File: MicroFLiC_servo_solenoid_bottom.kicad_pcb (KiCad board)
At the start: 2 copper layers, 49.8 x 49.8 mm, 49 parts, among them P1 Header_1x14, P10 Socket_1x4, P11 Header_R/A_2x3, P12 Header_R/A_2x3, P2 Socket_1x14, P3 12-way Micro-MaTch, P4 Jack_3.5mm_3pin, P5 Jack_3.5mm_3pin, P6 RCA_3, P7 RCA_3, P8 Socket_1x6, P9 Header_1x4, U1 PCA9306, U2 DRV103, U3 DRV103, U4 MCP4728

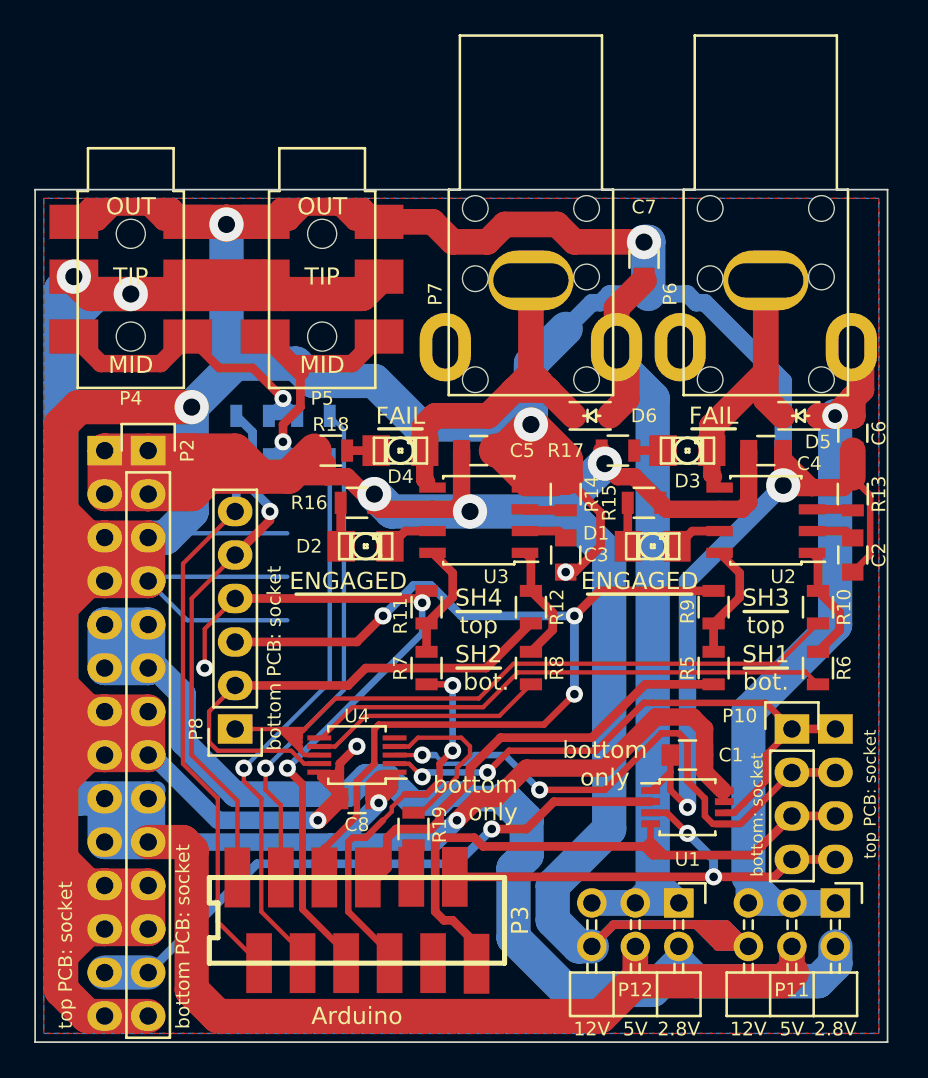
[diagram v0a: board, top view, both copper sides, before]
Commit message: Deleted redundant resistors and labels from PCB
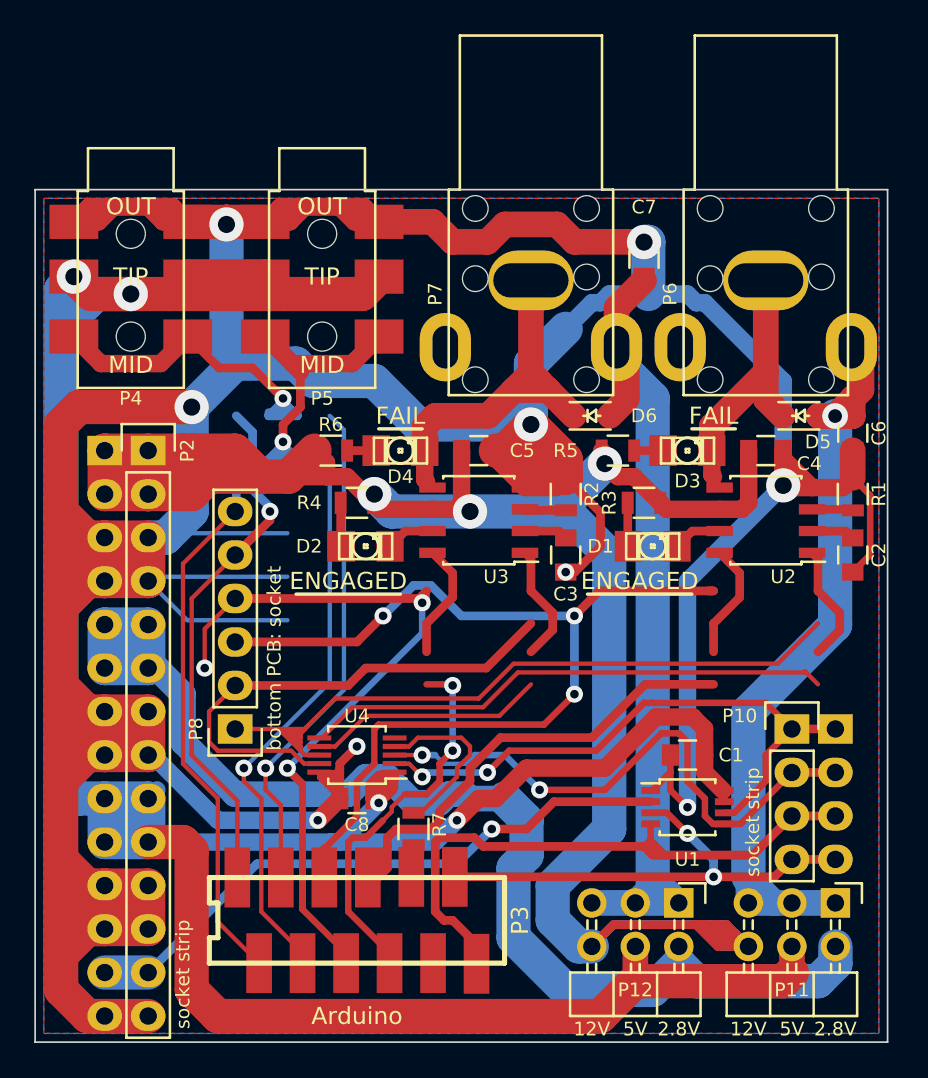
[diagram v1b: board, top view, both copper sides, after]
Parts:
- removed the R1 at (116.3, 113.3)
- removed R10, R11, R12, R8, R9: 0R, Resistors_SMD:R_0805
- removed the R2 at (112.8, 113.3)
- removed the R3 at (116.3, 115.8)
- removed the R4 at (112.8, 115.8)
- removed the R5 at (139.7, 128.0)
- removed the R6 at (145.8, 128.0)
- removed the R7 at (122.9, 128.0)
- C6, C7: value 10u/25V -> 4u7/25V
- D1, D2: value YELLOW -> LED RED
- D3, D4: value RED -> LED YELLOW
- D5, D6: value PMEG2020 -> 1N4148
- P1: value Header_1x14 -> 1x14 header strip
- P10: value Socket_1x4 -> 1x4 socket strip
- P11, P12: value Header_R/A_2x3 -> 2x3 header strip R/A
- P2: value Socket_1x14 -> 1x14 socket strip
- P8: value Socket_1x6 -> 1x6 socket strip
- P9: value Header_1x4 -> 1x4 header strip
- U1: value PCA9306 -> PCA9306DP
- renumbered R13 to R1, R14 to R2, R15 to R3, R16 to R4, R17 to R5, R18 to R6, R19 to R7
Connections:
- net /shutterPWM/SH3 renamed /SH3
- net /shutterPWM/SH4 renamed /SH4
- D5 pad 1: /shutterPWM/SHA_O/C -> /shutterPWM/SHA_PWR
- D5 pad 2: /shutterPWM/SHA_PWR -> /shutterPWM/SHA_O/C
- D6 pad 1: /shutterPWM/SHB_O/C -> /shutterPWM/SHB_PWR
- D6 pad 2: /shutterPWM/SHB_PWR -> /shutterPWM/SHB_O/C
- P4 pad 2: /SERVOA -> /SERVO1
- P5 pad 2: /SERVOB -> /SERVO2
- U2 pad 1: /shutterPWM/SHA_PWM -> /shutterPWM/SH1_PWM
- U2 pad 8: /shutterPWM/SHA_IN -> /shutterPWM/SH1
- U3 pad 1: /shutterPWM/SHB_PWM -> /shutterPWM/SH2_PWM
- U3 pad 8: /shutterPWM/SHB_IN -> /shutterPWM/SH2
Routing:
- net /SERVO1: track 29.8 -> 50.6 mm, vias 1 -> 2
- net /SERVOA: track 20.8 -> 0.00 mm, vias 1 -> 0
- net /SERVOB: track 18.8 -> 0.00 mm, vias 1 -> 0
- net /SERVO2: track 32.9 -> 51.7 mm, vias 1 -> 2
- net /shutterPWM/SHB_O/C: track 23.2 -> 10.6 mm
- net /shutterPWM/SHB_PWR: track 49.2 -> 61.8 mm
- net /shutterPWM/SHA_PWM: track 6.98 -> 0.00 mm
- net /shutterPWM/SH1_PWM: track 31.2 -> 38.2 mm
- net /shutterPWM/SH2_PWM: track 13.9 -> 20.8 mm
- net /shutterPWM/SHB_PWM: track 6.98 -> 0.00 mm
- net /shutterPWM/SHA_IN: track 6.90 -> 0.00 mm
- net /shutterPWM/SH1: track 31.6 -> 38.5 mm
- net /shutterPWM/SHB_IN: track 6.90 -> 0.00 mm
- net /shutterPWM/SH2: track 23.6 -> 30.5 mm
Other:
- board text added: "COIL 1"
- board text added: "COIL 2"
- board text added: "SERVO 1"
- board text added: "SERVO 2"
- board text added: "header strip"
- board text added: "socket strip"
- board text removed: "1&2"
- board text removed: "3&4"
- board text removed: "SERVOS"
- board text removed: "SH1 bot."
- board text removed: "SH2 bot."
- board text removed: "SH3 top"
- board text removed: "SH4 top"
- board text removed: "bottom PCB: pin header"
- board text removed: "bottom only"
- board text removed: "bottom: 1"
- board text removed: "bottom: 2"
- board text removed: "bottom: socket"
- board text removed: "top PCB: socket"
- board text removed: "top only"
- board text removed: "top: 3"
- board text removed: "top: 3 bottom: 1"
- board text removed: "top: 4"
- board text removed: "top: 4 bottom: 2"
- board text removed: "top: pin header"
